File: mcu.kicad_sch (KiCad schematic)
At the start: 13 parts, among them J6 Conn_02x05_Odd_Even

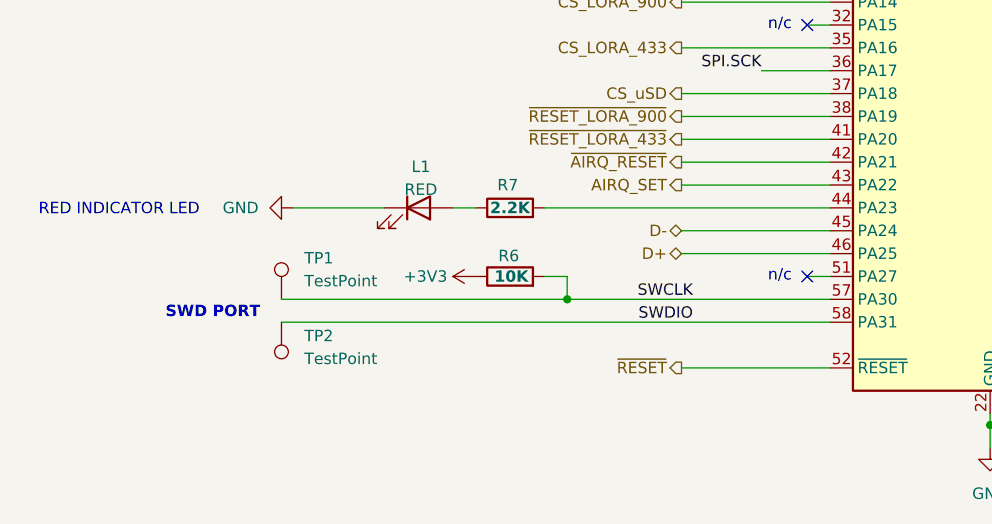
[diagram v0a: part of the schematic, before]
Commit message: Connected all signals except Buses
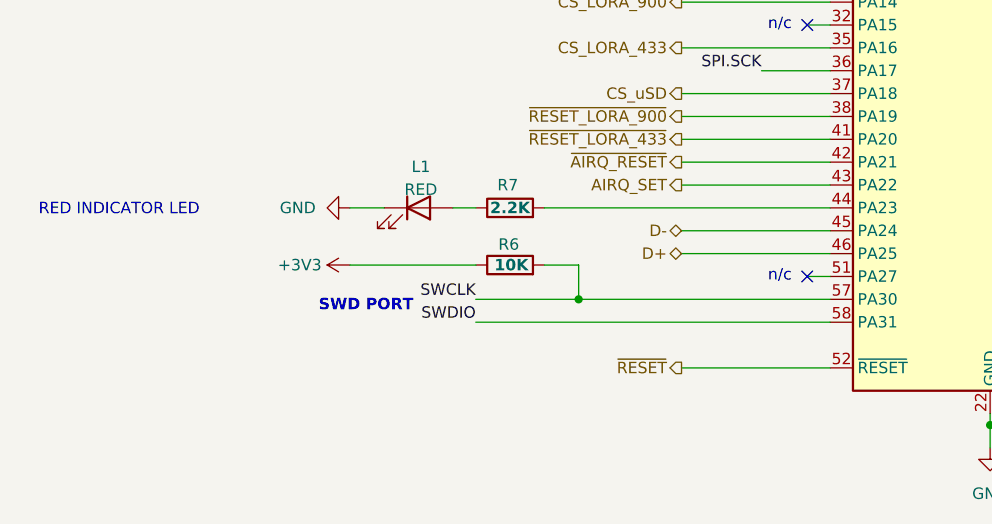
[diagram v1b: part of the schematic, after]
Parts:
- removed TP1, TP2: TestPoint, TestPoint:TestPoint_Pad_D1.5mm, symbol Connector:TestPoint

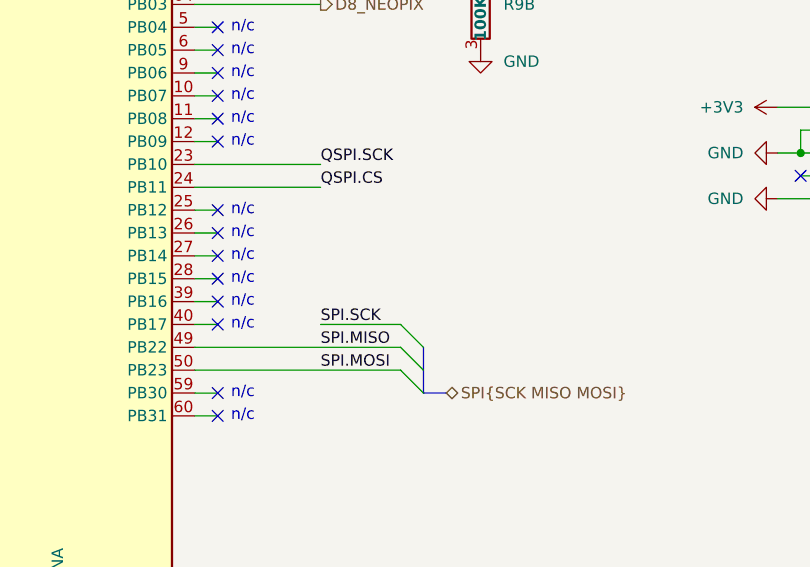
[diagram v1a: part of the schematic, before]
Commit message: Added mounting holes
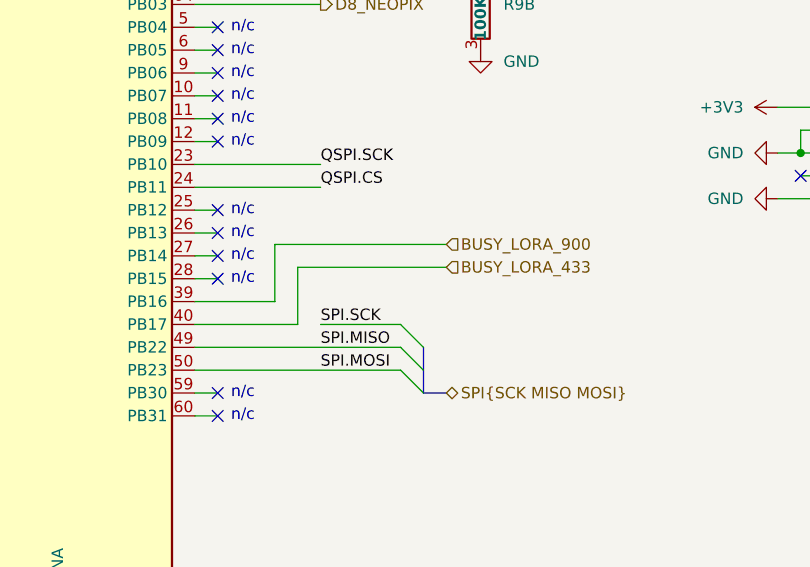
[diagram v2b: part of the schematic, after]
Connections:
- net BUSY_LORA_900: now reaches MCU1.39 (PB16)
- net BUSY_LORA_433: now reaches MCU1.40 (PB17)
- no-connect marks 26 -> 24
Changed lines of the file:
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@@
+	)
+	(no_connect
+		(at 173.99 99.06)
+	)
+	(no_connect
+		(at 173.99 101.6)
+	)
+	(no_connect
+		(at 173.99 91.44)
+	)
+	(no_connect
+		(at 264.16 92.71)
+	)
+	(no_connect
+		(at 173.99 81.28)
+	)
+	(no_connect
+		(at 133.35 132.08)
+	)
+	(no_connect
+		(at 173.99 106.68)
+	)
+	(no_connect
+		(at 133.35 71.12)
+	)
+	(no_connect
+		(at 173.99 119.38)
+	)
+	(no_connect
+		(at 173.99 86.36)
+	)
+	(no_connect
+		(at 173.99 68.58)
+	)
+	(no_connect
+		(at 133.35 78.74)
 	)
 	(no_connect
 		(at 173.99 88.9)
-	)
-	(no_connect
-		(at 173.99 99.06)
-	)
-	(no_connect
-		(at 173.99 91.44)
-	)
-	(no_connect
-		(at 173.99 101.6)
-	)
-	(no_connect
-		(at 173.99 111.76)
-	)
-	(no_connect
-		(at 264.16 92.71)
-	)
-	(no_connect
-		(at 173.99 109.22)
-	)
-	(no_connect
-		(at 173.99 81.28)
-	)
-	(no_connect
-		(at 133.35 132.08)
-	)
-	(no_connect
-		(at 173.99 106.68)
-	)
-	(no_connect
-		(at 133.35 71.12)
-	)
-	(no_connect
-		(at 173.99 119.38)
-	)
-	(no_connect
-		(at 173.99 86.36)
-	)
-	(no_connect
-		(at 173.99 68.58)
-	)
-	(no_connect
-		(at 133.35 78.74)
 	)
 	(bus_entry
@@
 	(wire
 		(pts
+			(xy 199.39 105.41) (xy 182.88 105.41)
+		)
+		(stroke
+			(width 0)
+			(type default)
+		)
+	)
+	(wire
+		(pts
 			(xy 133.35 78.74) (xy 135.89 78.74)
 		)
@@
 	(wire
 		(pts
+			(xy 171.45 88.9) (xy 173.99 88.9)
+		)
+		(stroke
+			(width 0)
+			(type default)
+		)
+	)
+	(wire
+		(pts
 			(xy 134.62 40.64) (xy 135.89 40.64)
 		)
@@
 	(wire
 		(pts
+			(xy 171.45 91.44) (xy 173.99 91.44)
+		)
+		(stroke
+			(width 0)
+			(type default)
+		)
+	)
+	(wire
+		(pts
 			(xy 153.67 52.07) (xy 153.67 55.88)
 		)
@@
 	(wire
 		(pts
-			(xy 171.45 91.44) (xy 173.99 91.44)
-		)
-		(stroke
-			(width 0)
-			(type default)
-		)
-	)
-	(wire
-		(pts
 			(xy 163.83 52.07) (xy 163.83 55.88)
 		)
@@
 	(wire
 		(pts
-			(xy 171.45 111.76) (xy 173.99 111.76)
+			(xy 171.45 111.76) (xy 182.88 111.76)
+		)
+		(stroke
+			(width 0)
+			(type default)
+		)
+	)
+	(wire
+		(pts
+			(xy 180.34 102.87) (xy 180.34 109.22)
 		)
 		(stroke
@@
 	(wire
 		(pts
-			(xy 171.45 88.9) (xy 173.99 88.9)
-		)
-		(stroke
-			(width 0)
-			(type default)
-		)
-	)
-	(wire
-		(pts
 			(xy 119.38 68.58) (xy 135.89 68.58)
 		)
@@
 	(wire
 		(pts
-			(xy 171.45 109.22) (xy 173.99 109.22)
+			(xy 180.34 102.87) (xy 199.39 102.87)
 		)
 		(stroke
@@
 	(wire
 		(pts
+			(xy 182.88 105.41) (xy 182.88 111.76)
+		)
+		(stroke
+			(width 0)
+			(type default)
+		)
+	)
+	(wire
+		(pts
 			(xy 203.2 73.66) (xy 203.2 71.12)
 		)
@@
 	(wire
 		(pts
+			(xy 180.34 109.22) (xy 171.45 109.22)
+		)
+		(stroke
+			(width 0)
+			(type default)
+		)
+	)
+	(wire
+		(pts
 			(xy 106.68 81.28) (xy 119.38 81.28)
 		)
@@
 	(text "n/c"
 		(exclude_from_sim no)
-		(at 176.784 111.76 0)
-		(effects
-			(font
-				(size 1.27 1.27)
-			)
-		)
-	)
-	(text "n/c"
-		(exclude_from_sim no)
 		(at 130.302 81.28 0)
 		(effects
@@
 	(text "n/c"
 		(exclude_from_sim no)
-		(at 176.784 109.22 0)
+		(at 176.784 88.9 0)
 		(effects
 			(font
@@
 	(text "n/c"
 		(exclude_from_sim no)
+		(at 176.784 91.44 0)
+		(effects
+			(font
+				(size 1.27 1.27)
+			)
+		)
+	)
+	(text "n/c"
+		(exclude_from_sim no)
 		(at 130.302 132.08 0)
 		(effects
@@
 	(text "n/c"
 		(exclude_from_sim no)
-		(at 176.784 88.9 0)
-		(effects
-			(font
-				(size 1.27 1.27)
-			)
-		)
-	)
-	(text "n/c"
-		(exclude_from_sim no)
 		(at 176.784 83.82 0)
 		(effects
@@
 		(exclude_from_sim no)
 		(at 176.784 106.68 0)
-		(effects
-			(font
-				(size 1.27 1.27)
-			)
-		)
-	)
-	(text "n/c"
-		(exclude_from_sim no)
-		(at 176.784 91.44 0)
 		(effects
 			(font
@@
 		(fields_autoplaced yes)
 		(effects
+			(font
+				(size 1.27 1.27)
+			)
+			(justify left)
+		)
+	)
+	(hierarchical_label "BUSY_LORA_900"
+		(shape input)
+		(at 199.39 102.87 0)
+		(fields_autoplaced yes)
+		(effects
+			(font
+				(size 1.27 1.27)
+			)
+			(justify left)
+		)
+	)
+	(hierarchical_label "BUSY_LORA_433"
+		(shape input)
+		(at 199.39 105.41 0)
+		(fields_autoplaced yes)
+		(effects

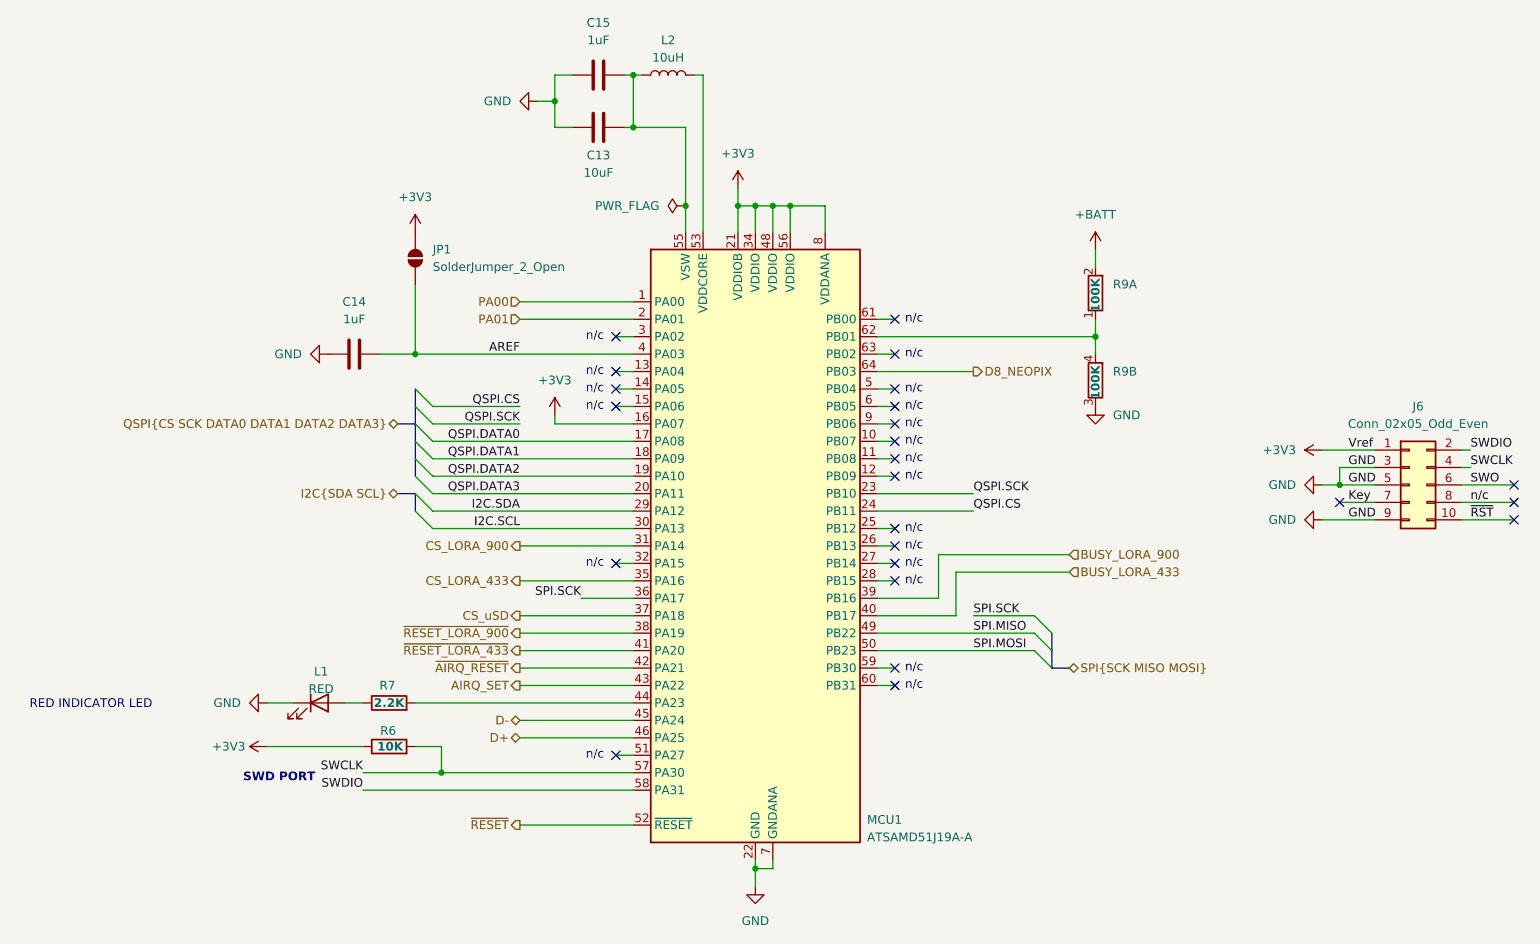
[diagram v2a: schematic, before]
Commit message: Cleaning up traces
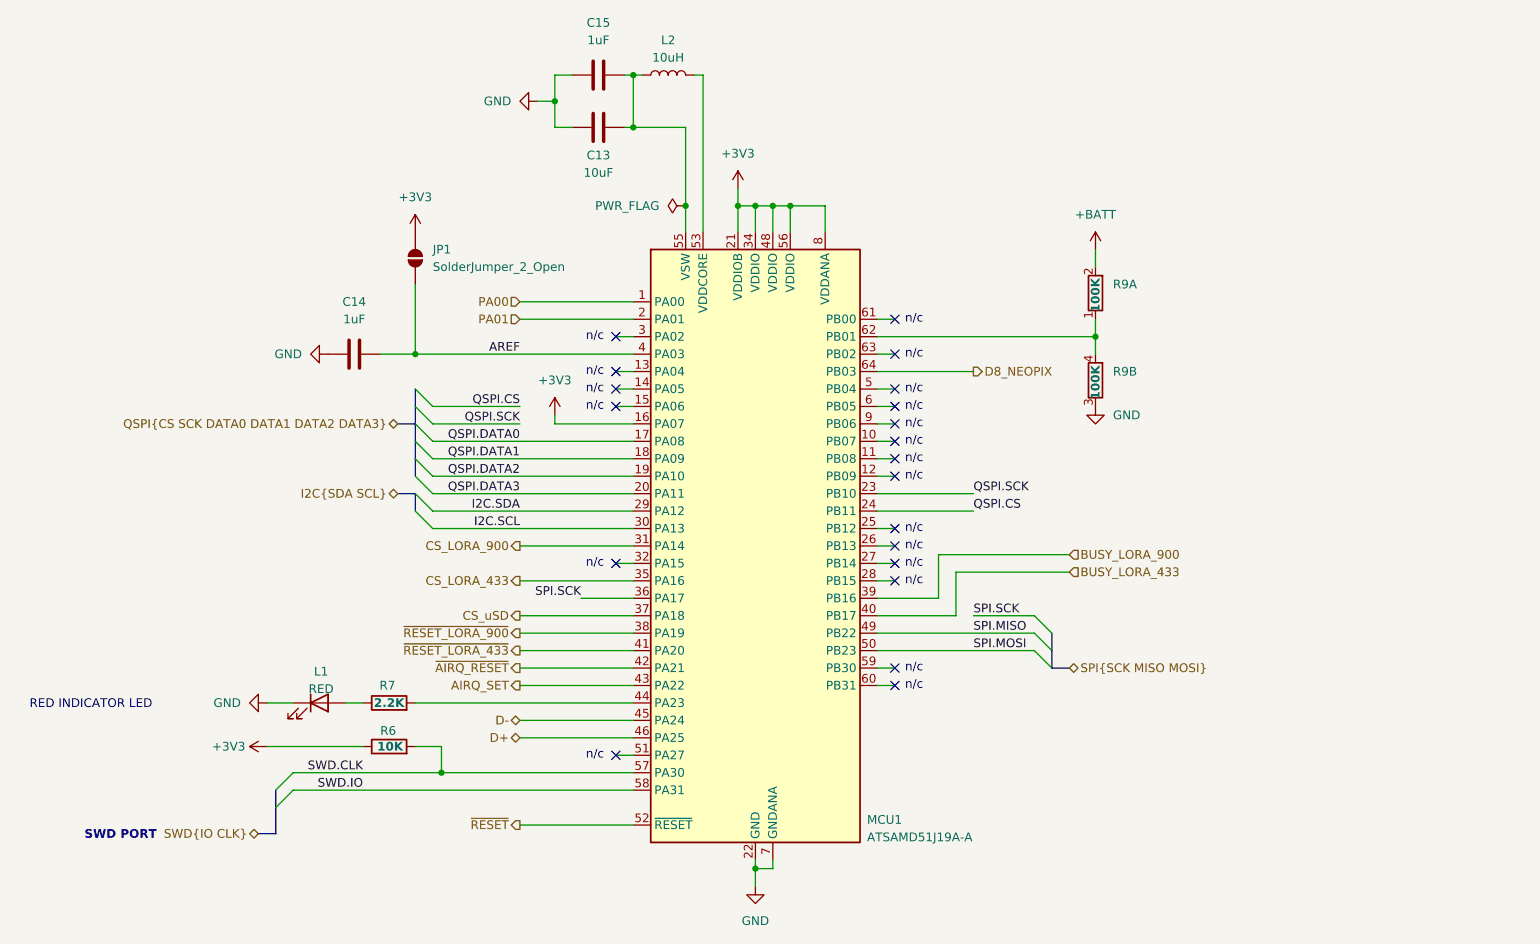
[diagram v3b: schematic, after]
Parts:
- removed J6: Conn_02x05_Odd_Even, Connector_PinHeader_1.27mm:PinHeader_2x05_P1.27mm_Vertical_SMD, symbol Connector_Generic:Conn_02x05_Odd_Even
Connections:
- net SWCLK renamed SWD.CLK
- net SWDIO renamed SWD.IO
- no-connect marks 24 -> 20

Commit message: Creating fab package
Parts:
- MCU1: Supplier_1 Unit Price $5.68 -> 5.68
- R9: value 100K -> 4x 100K
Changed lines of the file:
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@@
 			)
 		)
-		(property "Supplier_1 Unit Price" "$5.68"
+		(property "Supplier_1 Unit Price" "5.68"
 			(at 153.67 101.6 0)
 			(effects
@@
 			)
 		)
-		(property "Value" "100K"
+		(property "Value" "4x 100K"
 			(at 203.2 67.564 90)
 			(effects
@@
 			)
 		)
-		(property "Value" "100K"
+		(property "Value" "4x 100K"
 			(at 203.2 80.264 90)
 			(effects
